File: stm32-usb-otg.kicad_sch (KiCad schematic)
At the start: 42 parts, among them J1 USB_B_Micro, J2 Screw_Terminal_01x02, J3 Conn_02x05_Odd_Even, J4 Conn_01x04, J5 Conn_01x04, Q1 AO3401A, SW1 SW_SPDT, U1 MP2359, U2 STM32F405RGT6, U3 USBLC6-2SC6, Y1 16MHz

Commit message: Solved all Warnings !
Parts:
- J3: value Conn_02x05_Odd_Even -> SWD
- J4: value Conn_01x04 -> I2C Connector
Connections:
- net I2C1_SCLK: now also J4.2 (Pin_2), R5.2
- net I2C1_SDA: no longer U2.46 (PA13)
- removed net I2C1_SCKL: J4.2 (Pin_2), R5.2, U2.49 (PA14)
- net SWCLK renamed SWD_SCLK
- net SWD_SCLK: now also U2.49 (PA14)
- net SWDIO renamed SWD_SWDIO
- net SWD_SWDIO: now also U2.46 (PA13)
- no-connect marks 47 -> 45
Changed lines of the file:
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@@
   (no_connect (at 140.97 139.7))
   (no_connect (at 140.97 142.24))
-  (no_connect (at 140.97 143.51))
   (no_connect (at 140.97 144.78))
   (no_connect (at 228.6 104.14))
@@
   (no_connect (at 241.3 101.6))
   (no_connect (at 228.6 130.81))
-  (no_connect (at 270.51 127))
   (wire (pts (xy 99.06 115.57) (xy 99.06 111.76))
     (stroke (width 0) (type default) (color 0 0 0 0))
@@
     )
   )
-  (global_label "I2C1_SCKL" (shape input) (at 185.42 156.21 180) (fields_autoplaced)
+  (global_label "I2C1_SCLK" (shape input) (at 185.42 156.21 180) (fields_autoplaced)
     (effects (font (size 1.27 1.27)) (justify right))
     (property "Intersheet References" "${INTERSHEET_REFS}" (id 0) (at 172.9679 156.1306 0)
@@
     )
   )
-  (global_label "SWDIO" (shape input) (at 252.73 96.52 0) (fields_autoplaced)
+  (global_label "SWD_SWDIO" (shape input) (at 252.73 96.52 0) (fields_autoplaced)
     (effects (font (size 1.27 1.27)) (justify left))
-    (property "Intersheet References" "${INTERSHEET_REFS}" (id 0) (at 261.0093 96.4406 0)
+    (property "Intersheet References" "${INTERSHEET_REFS}" (id 0) (at 265.9079 96.4406 0)
       (effects (font (size 1.27 1.27)) (justify left) hide)
     )
@@
     )
   )
-  (global_label "I2C1_SCKL" (shape input) (at 144.78 129.54 0) (fields_autoplaced)
+  (global_label "SWD_SCLK" (shape input) (at 144.78 129.54 0) (fields_autoplaced)
     (effects (font (size 1.27 1.27)) (justify left))
-    (property "Intersheet References" "${INTERSHEET_REFS}" (id 0) (at 157.2321 129.4606 0)
+    (property "Intersheet References" "${INTERSHEET_REFS}" (id 0) (at 156.8693 129.4606 0)
       (effects (font (size 1.27 1.27)) (justify left) hide)
     )
@@
     )
   )
-  (global_label "I2C1_SCKL" (shape input) (at 228.6 147.32 180) (fields_autoplaced)
+  (global_label "I2C1_SCLK" (shape input) (at 228.6 147.32 180) (fields_autoplaced)
     (effects (font (size 1.27 1.27)) (justify right))
     (property "Intersheet References" "${INTERSHEET_REFS}" (id 0) (at 216.1479 147.2406 0)
@@
     )
   )
-  (global_label "I2C1_SDA" (shape input) (at 156.21 127 0) (fields_autoplaced)
+  (global_label "SWD_SWDIO" (shape input) (at 156.21 127 0) (fields_autoplaced)
     (effects (font (size 1.27 1.27)) (justify left))
-    (property "Intersheet References" "${INTERSHEET_REFS}" (id 0) (at 167.4526 126.9206 0)
+    (property "Intersheet References" "${INTERSHEET_REFS}" (id 0) (at 169.3879 126.9206 0)
       (effects (font (size 1.27 1.27)) (justify left) hide)
     )
@@
     )
   )
-  (global_label "SWCLK" (shape input) (at 264.16 99.06 0) (fields_autoplaced)
+  (global_label "SWD_SCLK" (shape input) (at 264.16 99.06 0) (fields_autoplaced)
     (effects (font (size 1.27 1.27)) (justify left))
-    (property "Intersheet References" "${INTERSHEET_REFS}" (id 0) (at 272.8021 98.9806 0)
+    (property "Intersheet References" "${INTERSHEET_REFS}" (id 0) (at 276.2493 98.9806 0)
       (effects (font (size 1.27 1.27)) (justify left) hide)
     )
@@
     (in_bom yes) (on_board yes)
     (property "Reference" "J3" (id 0) (at 234.95 93.98 0))
-    (property "Value" "Conn_02x05_Odd_Even" (id 1) (at 234.95 109.22 0))
+    (property "Value" "SWD" (id 1) (at 234.95 109.22 0))
     (property "Footprint" "" (id 2) (at 233.68 101.6 0)
       (effects (font (size 1.27 1.27)) hide)
@@
       (effects (font (size 1.27 1.27)) (justify left))
     )
-    (property "Value" "Conn_01x04" (id 1) (at 233.68 154.94 0)
+    (property "Value" "I2C Connector" (id 1) (at 233.68 154.94 0)
       (effects (font (size 1.27 1.27)) (justify left))
     )
@@
     )
     (path "/0b7e1823-6eac-4b15-b3be-85dcf20f7791"
-      (reference "J3") (unit 1) (value "Conn_02x05_Odd_Even") (footprint "")
+      (reference "J3") (unit 1) (value "SWD") (footprint "")
     )
     (path "/c31c5d1b-f330-4b15-afa3-c869372eecb1"
-      (reference "J4") (unit 1) (value "Conn_01x04") (footprint "")
+      (reference "J4") (unit 1) (value "I2C Connector") (footprint "")
     )
     (path "/07fb7041-aa81-4dba-a8b3-1c14102f2cd4"

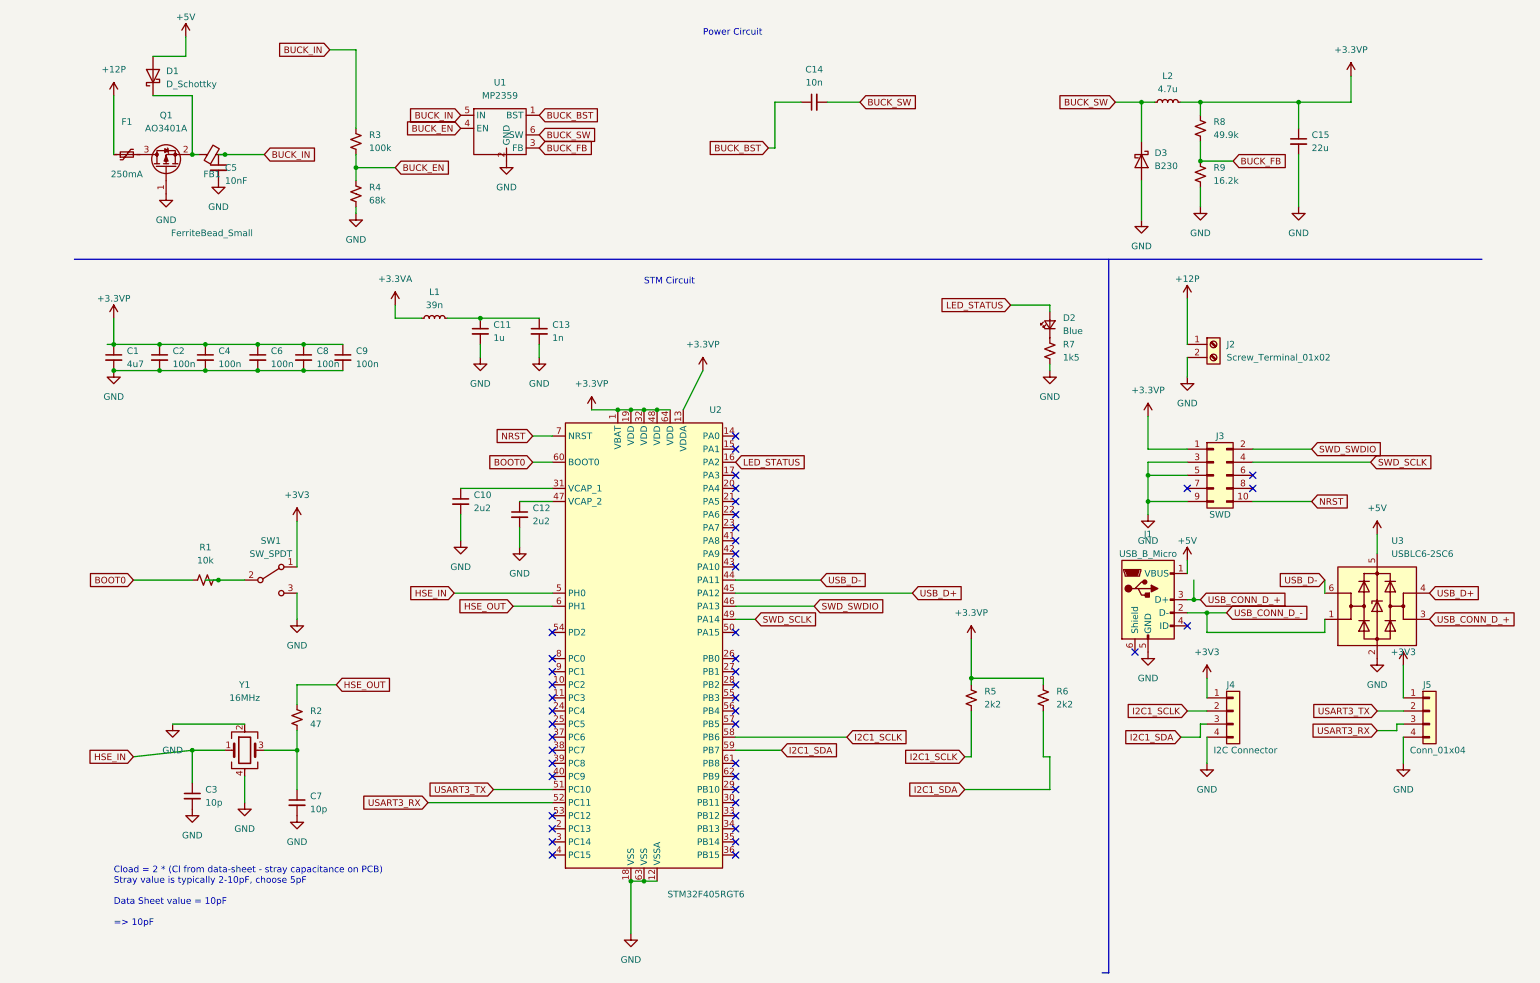
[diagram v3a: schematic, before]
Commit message: Solved all errors by adding "Power flag" connectors.
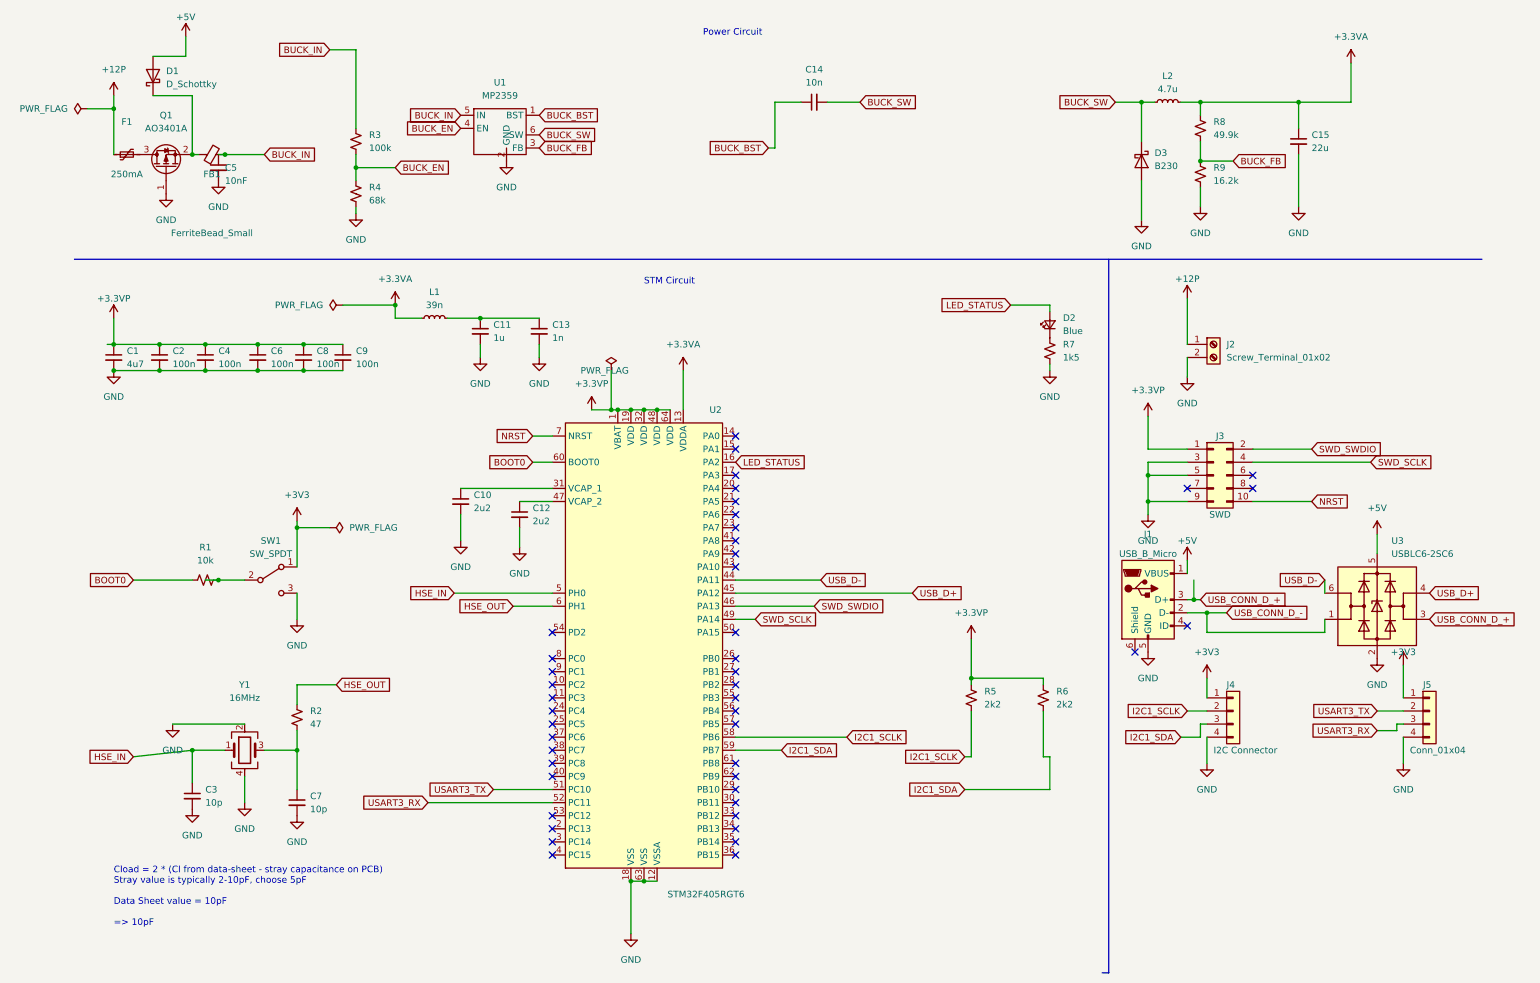
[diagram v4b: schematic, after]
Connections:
- net +3.3VA: now also C15.1, L2.2, R8.1, U2.13 (VDDA)
- net +3.3VP: no longer C15.1, L2.2, R8.1, U2.13 (VDDA)

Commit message: Generated a net-list.
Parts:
- C1: footprint Capacitor_SMD:CP_Elec_3x5.3 -> Capacitor_SMD:C_0402_1005Metric
- C10, C14, C15, C5: footprint (none) -> Capacitor_SMD:C_1206_3216Metric
- C11, C12, C13, C2, C3, C4, C6, C7, C8, C9: footprint (none) -> Capacitor_SMD:C_0402_1005Metric
- D1: footprint (none) -> Diode_SMD:D_SOD-123
- D2: footprint (none) -> LED_SMD:LED_0603_1608Metric
- F1: footprint (none) -> Fuse:Fuse_0402_1005Metric
- FB1: footprint (none) -> Inductor_SMD:L_0805_2012Metric
- J1: footprint (none) -> Connector_USB:USB_B_Amphenol_MUSB-D511_Vertical_Rugged
- J2: footprint (none) -> TerminalBlock_Phoenix:TerminalBlock_Phoenix_MKDS-3-2-5.08_1x02_P5.08mm_Horizontal
- J3: footprint (none) -> Connector_PinHeader_1.00mm:PinHeader_2x05_P1.00mm_Vertical_SMD
- J4, J5: footprint (none) -> Connector:FanPinHeader_1x04_P2.54mm_Vertical
- L1, L2: footprint (none) -> Inductor_SMD:L_0402_1005Metric
- R1, R2, R3, R4, R5, R6, R7, R8, R9: footprint (none) -> Resistor_SMD:R_0402_1005Metric
- SW1: footprint (none) -> Button_Switch_SMD:SW_SPST_Panasonic_EVQPL_3PL_5PL_PT_A08
- U1: footprint (none) -> Package_TO_SOT_THT:TO-5-6
- Y1: footprint (none) -> Crystal:Crystal_AT310_D3.0mm_L10.0mm_Horizontal
